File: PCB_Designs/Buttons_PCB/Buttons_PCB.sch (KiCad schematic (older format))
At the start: 66 parts, among them U1 MCDTS2-4N, U10 MCDTS2-4N, U11 MCDTS2-4N, U12 MCDTS2-4N, U13 MCP23017, U14 MCP23017, U2 MCDTS2-4N, U3 MCDTS2-4N, U4 MCDTS2-4N, U5 MCDTS2-4N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

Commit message: Buttons PCB almost done
* Footprints for Cherry MX switches added
* Buttons.sch edited to finished schematic
* Buttons.net generated
* Buttons.kicad_pcb created and designed
* Uneccesary files deleted
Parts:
- removed D1, D10, D11, D12, D2, D3, D4, D5, D6, D7, D8, D9: LED, symbol LED-RESCUE-Buttons_PCB
- removed U1, U10, U11, U12, U2, U3, U4, U5, U6, U7, U8, U9: MCDTS2-4N, symbol MCDTS2-4N
- added C16, C17: 100n, Capacitors_SMD:C_0603_HandSoldering, symbol C
- added D1, D10, D11, D12, D2, D3, D4, D5, D6, D7, D8, D9: LED_Small_ALT, Keyboard:CHERRY_MX_LED, symbol LED_Small_ALT
- added U1, U10, U11, U12, U2, U3, U4, U5, U6, U7, U8, U9: CHERRY-MX, Keyboard:CHERRY_PCB_100H, symbol CHERRY-MX
- C1, C10, C11, C12, C13, C14, C2, C3, C4, C5, C6, C7, C8, C9: footprint (none) -> Capacitors_SMD:C_0603_HandSoldering
- C15: footprint (none) -> Capacitors_SMD:CP_Elec_4x4.5
- P1: renamed from P?; footprint (none) -> Socket_Strips:Socket_Strip_Straight_1x06
- R1, R13, R14, R15, R16, R17, R18, R19, R2, R20, R21, R22, R23, R24: footprint (none) -> Resistors_SMD:R_0603_HandSoldering
- R10, R11, R12, R3, R4, R5, R6, R7, R8, R9: value 1k -> 10k; footprint (none) -> Resistors_SMD:R_0603_HandSoldering
- U13, U14: footprint (none) -> Housings_DIP:DIP-28_W7.62mm_SMDSocket_SmallPads
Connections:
- wire segments 79 -> 91
- no-connect marks 20 -> 8
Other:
- moved on the sheet: R1, R2, R3

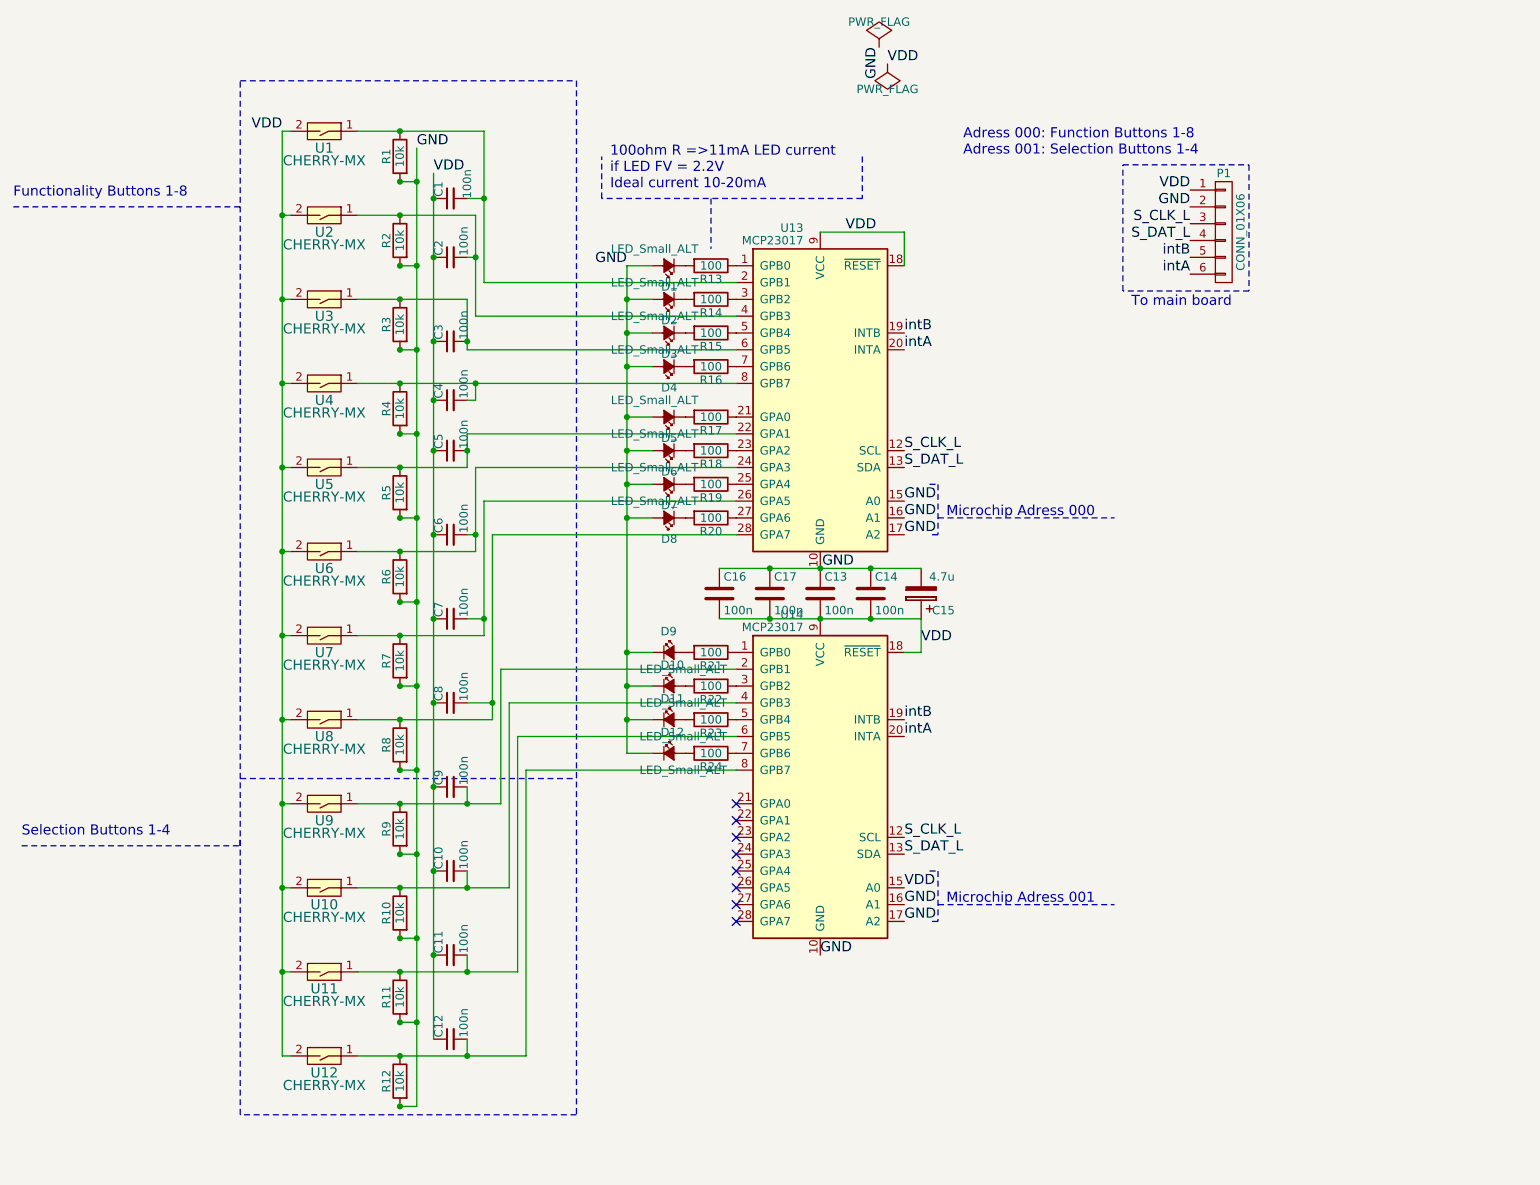
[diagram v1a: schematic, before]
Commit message: Buttons_PWB_1.0
First edition Buttons_PWB routed (V1.0).
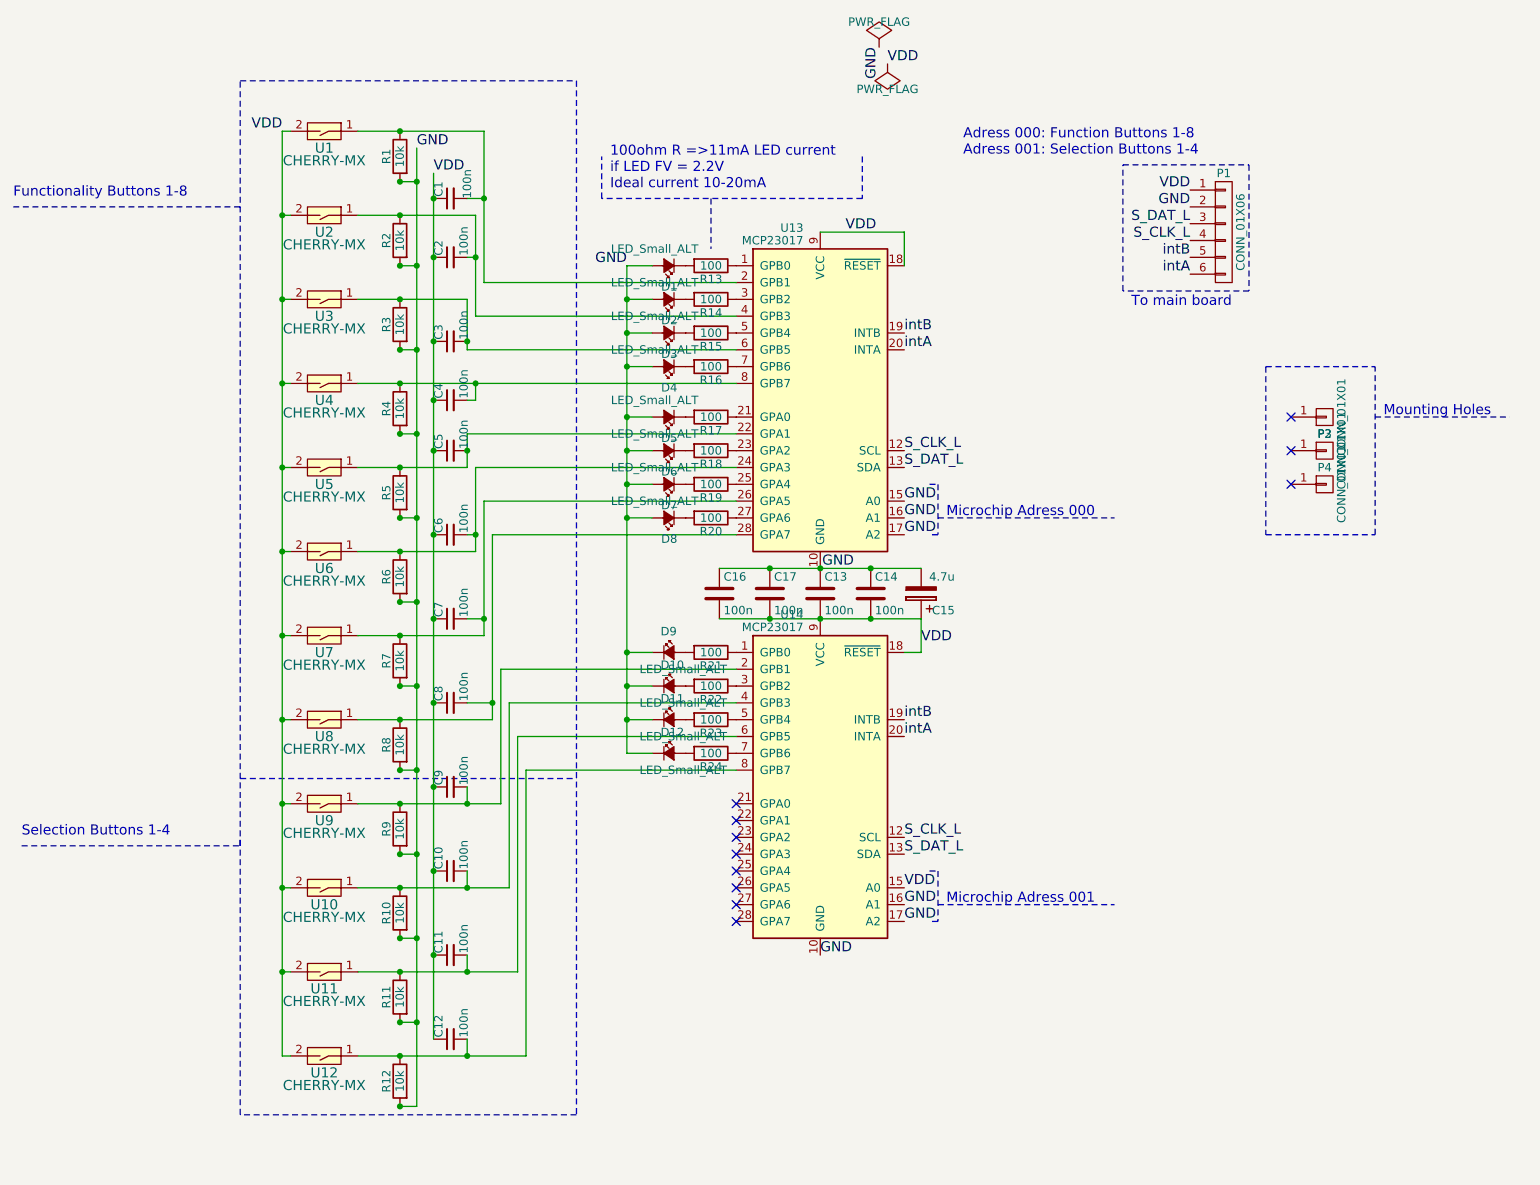
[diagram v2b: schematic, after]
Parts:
- added P2, P3, P4: CONN_01X01, Mounting_Holes:MountingHole_3mm, symbol CONN_01X01
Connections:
- net S_CLK_L: now also P1.4 (P4); no longer P1.3 (P3)
- net S_DAT_L: now also P1.3 (P3); no longer P1.4 (P4)
- no-connect marks 8 -> 11
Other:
- note added: "Mounting Holes"
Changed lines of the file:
@@
 Text Label 9000 1700 2    60   ~ 0
 GND
+Text Label 9000 1900 2    60   ~ 0
+S_CLK_L
 Text Label 9000 1800 2    60   ~ 0
-S_CLK_L
-Text Label 9000 1900 2    60   ~ 0
 S_DAT_L
 Text Label 9000 2100 2    60   ~ 0
@@
 	4050 2250 4700 2250
 Wire Wire Line
-	4050 3250 4700 3250
-Wire Wire Line
-	4050 3750 4750 3750
-Wire Wire Line
-	4050 4250 4800 4250
-Wire Wire Line
-	4050 4750 4850 4750
+	4700 3250 4050 3250
+Wire Wire Line
+	4750 3750 4050 3750
+Wire Wire Line
+	4800 4250 4050 4250
+Wire Wire Line
+	4850 4750 4050 4750
 Wire Wire Line
 	4050 5250 4900 5250
@@
 	4750 1750 4750 2350
 Wire Wire Line
-	4700 3250 4700 3050
-Wire Wire Line
-	4750 3750 4750 3250
-Wire Wire Line
-	4800 4250 4800 3450
-Wire Wire Line
-	4850 4750 4850 3650
+	4700 3050 4700 3250
+Wire Wire Line
+	4750 3250 4750 3750
+Wire Wire Line
+	4800 3450 4800 4250
+Wire Wire Line
+	4850 3650 4850 4750
 Wire Notes Line
 	3350 5100 5350 5100
@@
 Connection ~ 4300 7050
 Wire Wire Line
-	4400 7050 4400 1350
+	4400 1350 4400 7050
 Connection ~ 4300 1250
 Connection ~ 4400 1550
@@
 	4300 2550 4400 2550
 Wire Wire Line
-	4300 7050 4400 7050
+	4400 7050 4300 7050
 Wire Wire Line
 	4300 6550 4400 6550
@@
 Connection ~ 6500 4150
 Connection ~ 6800 4150
+$Comp
+L CONN_01X01 P2
+U 1 1 588FBE14
+P 9800 2950
+F 0 "P2" H 9800 3050 50  0000 C CNN
+F 1 "CONN_01X01" V 9900 2950 50  0000 C CNN
+F 2 "Mounting_Holes:MountingHole_3mm" H 9800 2950 50  0001 C CNN
+F 3 "" H 9800 2950 50  0001 C CNN
+	1    9800 2950
+	1    0    0    1
+$EndComp
+$Comp
+L CONN_01X01 P3
+U 1 1 588FBF5A
+P 9800 3150
+F 0 "P3" H 9800 3250 50  0000 C CNN
+F 1 "CONN_01X01" V 9900 3150 50  0000 C CNN
+F 2 "Mounting_Holes:MountingHole_3mm" H 9800 3150 50  0001 C CNN
+F 3 "" H 9800 3150 50  0001 C CNN
+	1    9800 3150
+	1    0    0    -1
+$EndComp
+$Comp
+L CONN_01X01 P4
+U 1 1 588FC040
+P 9800 3350
+F 0 "P4" H 9800 3450 50  0000 C CNN
+F 1 "CONN_01X01" V 9900 3350 50  0000 C CNN
+F 2 "Mounting_Holes:MountingHole_3mm" H 9800 3350 50  0001 C CNN
+F 3 "" H 9800 3350 50  0001 C CNN
+	1    9800 3350
+	1    0    0    -1
+$EndComp
+NoConn ~ 9600 2950
+NoConn ~ 9600 3150
+NoConn ~ 9600 3350
+Wire Notes Line
+	9450 2650 10100 2650
+Wire Notes Line
+	9450 2650 9450 3650
+Wire Notes Line
+	9450 3650 10100 3650
+Wire Notes Line
+	10100 3650 10100 2650
+Text Notes 10150 2950 0    60   ~ 0
+Mounting Holes
+Wire Notes Line
+	10100 2950 10900 2950
 $EndSCHEMATC

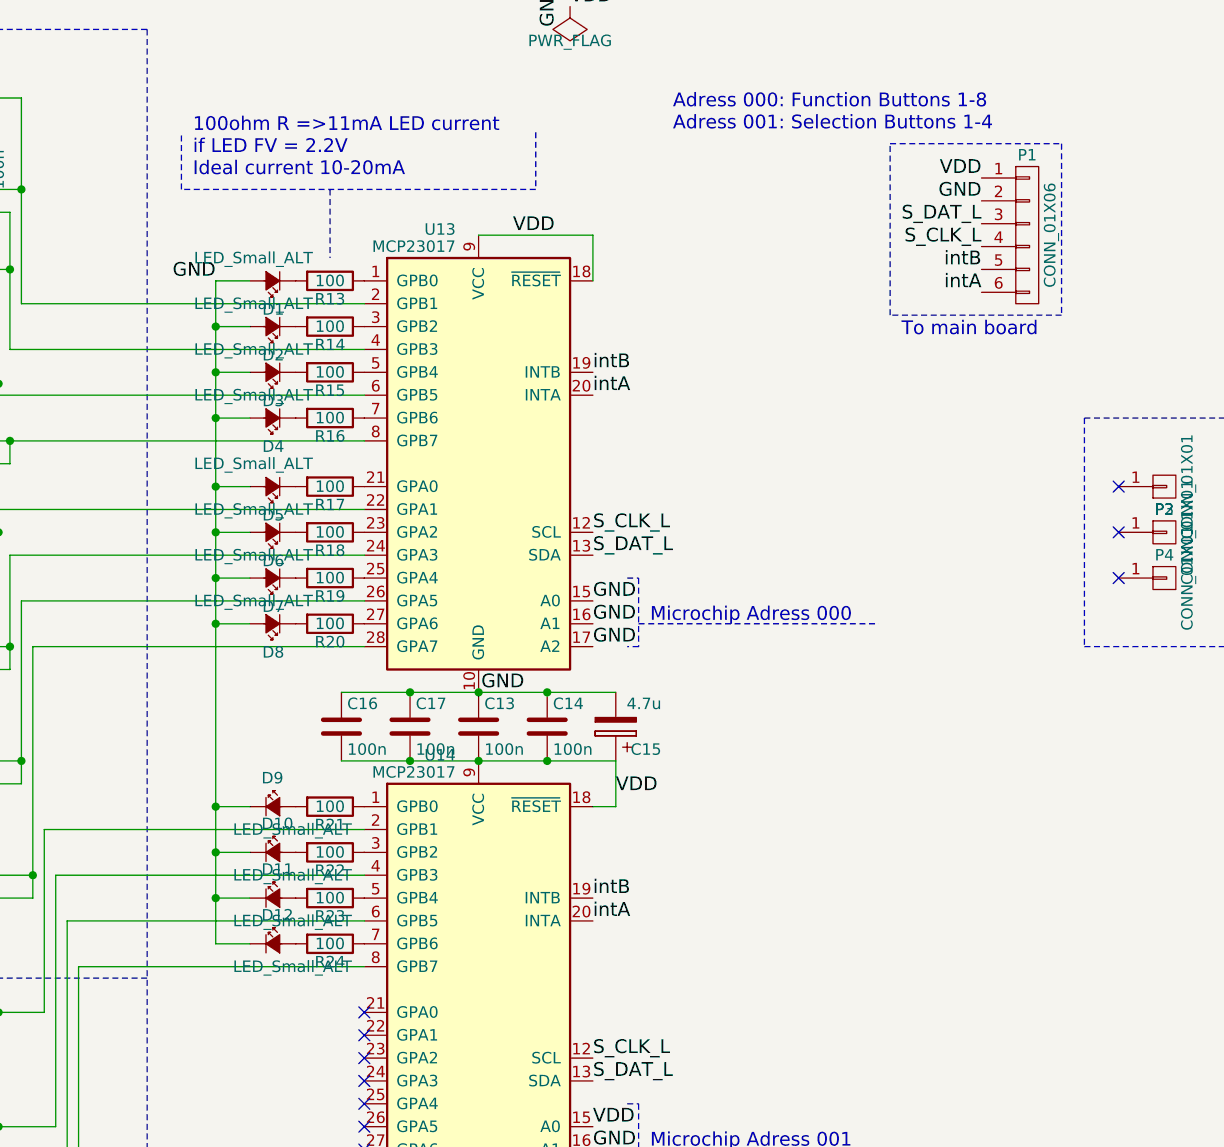
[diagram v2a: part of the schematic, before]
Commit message: Buttons_V3, Sliders_V2
Easier to manufacture External PCB designs finalized.
Uneccesary footprints library added "Connectors" (Could not find the
regular connector FP, turns out it's the socket-strips)
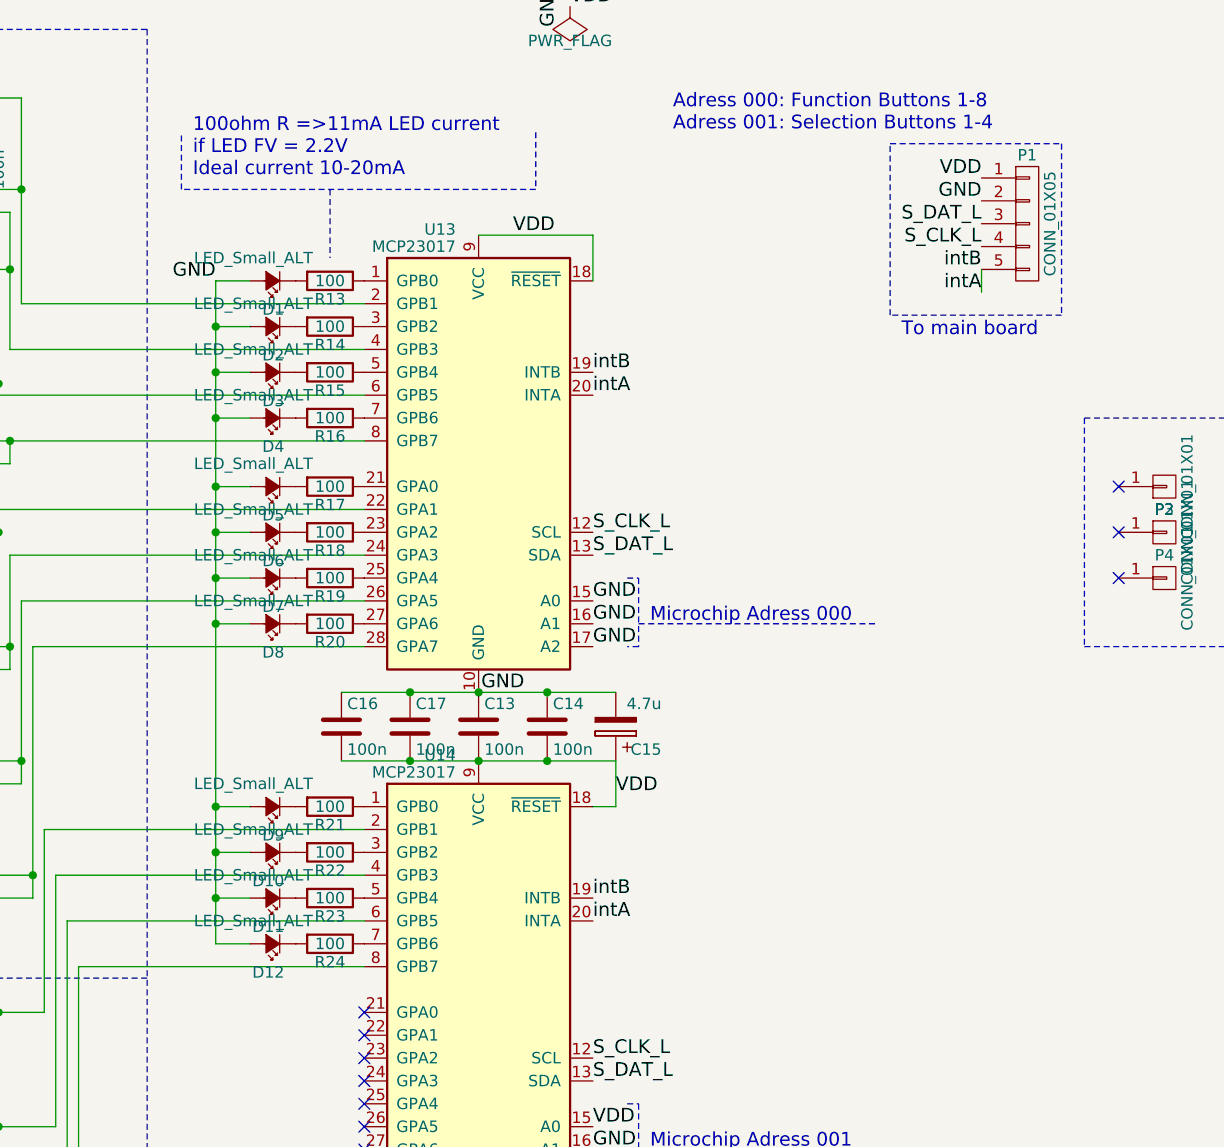
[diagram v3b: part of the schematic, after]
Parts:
- removed P1: CONN_01X06, Socket_Strips:Socket_Strip_Straight_1x06, symbol CONN_01X06
- added P1: CONN_01X05, Socket_Strips:Socket_Strip_Straight_1x05_Pitch2.54mm, symbol CONN_01X05
- P2, P3, P4: footprint Mounting_Holes:MountingHole_3mm -> Socket_Strips:Socket_Strip_Straight_1x01_Pitch2.54mm
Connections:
- net intB is gone; now on net intA: U13.19 (INTB), U14.19 (INTB)
- net GND: now also D10.2 (A), D11.2 (A), D12.2 (A), D9.2 (A), P1.2 (P2); no longer D10.1 (K), D11.1 (K), D12.1 (K), D9.1 (K)
- net S_CLK_L: now also P1.4 (P4)
- net S_DAT_L: now also P1.3 (P3)
- net VDD: now also P1.1 (P1)
- net intA: now also P1.5 (P5)
- net at R21.2: now also D9.1 (K); no longer D9.2 (A)
- net at R22.2: now also D10.1 (K); no longer D10.2 (A)
- net at R23.2: now also D11.1 (K); no longer D11.2 (A)
- net at R24.2: now also D12.1 (K); no longer D12.2 (A)
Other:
- moved on the sheet: D10, D11, D12, D9
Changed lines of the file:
@@
 VDD
 $Comp
-L CONN_01X06 P1
-U 1 1 588E7D95
-P 9200 1850
-F 0 "P1" H 9200 2200 50  0000 C CNN
-F 1 "CONN_01X06" V 9300 1850 50  0000 C CNN
-F 2 "Socket_Strips:Socket_Strip_Straight_1x06" H 9200 1850 50  0001 C CNN
-F 3 "" H 9200 1850 50  0000 C CNN
-	1    9200 1850
-	1    0    0    -1
-$EndComp
-$Comp
-L PWR_FLAG #FLG01
+L PWR_FLAG #FLG1
 U 1 1 588ED4C3
 P 7150 750
-F 0 "#FLG01" H 7150 825 50  0001 C CNN
+F 0 "#FLG1" H 7150 825 50  0001 C CNN
 F 1 "PWR_FLAG" H 7150 900 50  0000 C CNN
 F 2 "" H 7150 750 50  0001 C CNN
@@
 $EndComp
 $Comp
-L PWR_FLAG #FLG02
+L PWR_FLAG #FLG2
 U 1 1 588ED59B
 P 7200 850
-F 0 "#FLG02" H 7200 925 50  0001 C CNN
+F 0 "#FLG2" H 7200 925 50  0001 C CNN
 F 1 "PWR_FLAG" H 7200 1000 50  0000 C CNN
 F 2 "" H 7200 850 50  0001 C CNN
@@
 F 3 "" V 5900 4350 50  0001 C CNN
 	1    5900 4350
-	1    0    0    -1
+	-1   0    0    1
 $EndComp
 $Comp
@@
 F 3 "" V 5900 4550 50  0001 C CNN
 	1    5900 4550
-	1    0    0    -1
+	-1   0    0    1
 $EndComp
 $Comp
@@
 F 3 "" V 5900 4750 50  0001 C CNN
 	1    5900 4750
-	1    0    0    -1
+	-1   0    0    1
 $EndComp
 $Comp
@@
 F 3 "" V 5900 4950 50  0001 C CNN
 	1    5900 4950
-	1    0    0    -1
+	-1   0    0    1
 $EndComp
 $Comp
@@
 F 0 "P2" H 9800 3050 50  0000 C CNN
 F 1 "CONN_01X01" V 9900 2950 50  0000 C CNN
-F 2 "Mounting_Holes:MountingHole_3mm" H 9800 2950 50  0001 C CNN
+F 2 "Socket_Strips:Socket_Strip_Straight_1x01_Pitch2.54mm" H 9800 2950 50  0001 C CNN
 F 3 "" H 9800 2950 50  0001 C CNN
 	1    9800 2950
@@
 F 0 "P3" H 9800 3250 50  0000 C CNN
 F 1 "CONN_01X01" V 9900 3150 50  0000 C CNN
-F 2 "Mounting_Holes:MountingHole_3mm" H 9800 3150 50  0001 C CNN
+F 2 "Socket_Strips:Socket_Strip_Straight_1x01_Pitch2.54mm" H 9800 3150 50  0001 C CNN
 F 3 "" H 9800 3150 50  0001 C CNN
 	1    9800 3150
@@
 F 0 "P4" H 9800 3450 50  0000 C CNN
 F 1 "CONN_01X01" V 9900 3350 50  0000 C CNN
-F 2 "Mounting_Holes:MountingHole_3mm" H 9800 3350 50  0001 C CNN
+F 2 "Socket_Strips:Socket_Strip_Straight_1x01_Pitch2.54mm" H 9800 3350 50  0001 C CNN
 F 3 "" H 9800 3350 50  0001 C CNN
 	1    9800 3350
@@
 Wire Notes Line
 	10100 2950 10900 2950
+$Comp
+L CONN_01X05 P1
+U 1 1 589F628B
+P 9200 1800
+F 0 "P1" H 9200 2100 50  0000 C CNN
+F 1 "CONN_01X05" V 9300 1800 50  0000 C CNN
+F 2 "Socket_Strips:Socket_Strip_Straight_1x05_Pitch2.54mm" H 9200 1800 50  0001 C CNN
+F 3 "" H 9200 1800 50  0001 C CNN
+	1    9200 1800
+	1    0    0    -1
+$EndComp
+Wire Wire Line
+	9000 2100 9000 2000
 $EndSCHEMATC

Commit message: First PCB version of main board
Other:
- note added: "!!!!!!!!!!!!!!!!!!!"
- note added: "FIXA VDD<->R<->SWITCH<->R<->I/O_Exp"
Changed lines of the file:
@@
 VDD
 $Comp
-L PWR_FLAG #FLG1
+L PWR_FLAG #FLG01
 U 1 1 588ED4C3
 P 7150 750
-F 0 "#FLG1" H 7150 825 50  0001 C CNN
+F 0 "#FLG01" H 7150 825 50  0001 C CNN
 F 1 "PWR_FLAG" H 7150 900 50  0000 C CNN
 F 2 "" H 7150 750 50  0001 C CNN
@@
 $EndComp
 $Comp
-L PWR_FLAG #FLG2
+L PWR_FLAG #FLG02
 U 1 1 588ED59B
 P 7200 850
-F 0 "#FLG2" H 7200 925 50  0001 C CNN
+F 0 "#FLG02" H 7200 925 50  0001 C CNN
 F 1 "PWR_FLAG" H 7200 1000 50  0000 C CNN
 F 2 "" H 7200 850 50  0001 C CNN
@@
 Wire Wire Line
 	9000 2100 9000 2000
+Text Notes 3300 900  0    60   ~ 0
+FIXA VDD<->R<->SWITCH<->R<->I/O_Exp
+Text Notes 3300 800  0    60   ~ 0
+!!!!!!!!!!!!!!!!!!!
 $EndSCHEMATC
